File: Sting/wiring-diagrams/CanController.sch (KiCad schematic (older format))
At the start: 57 parts

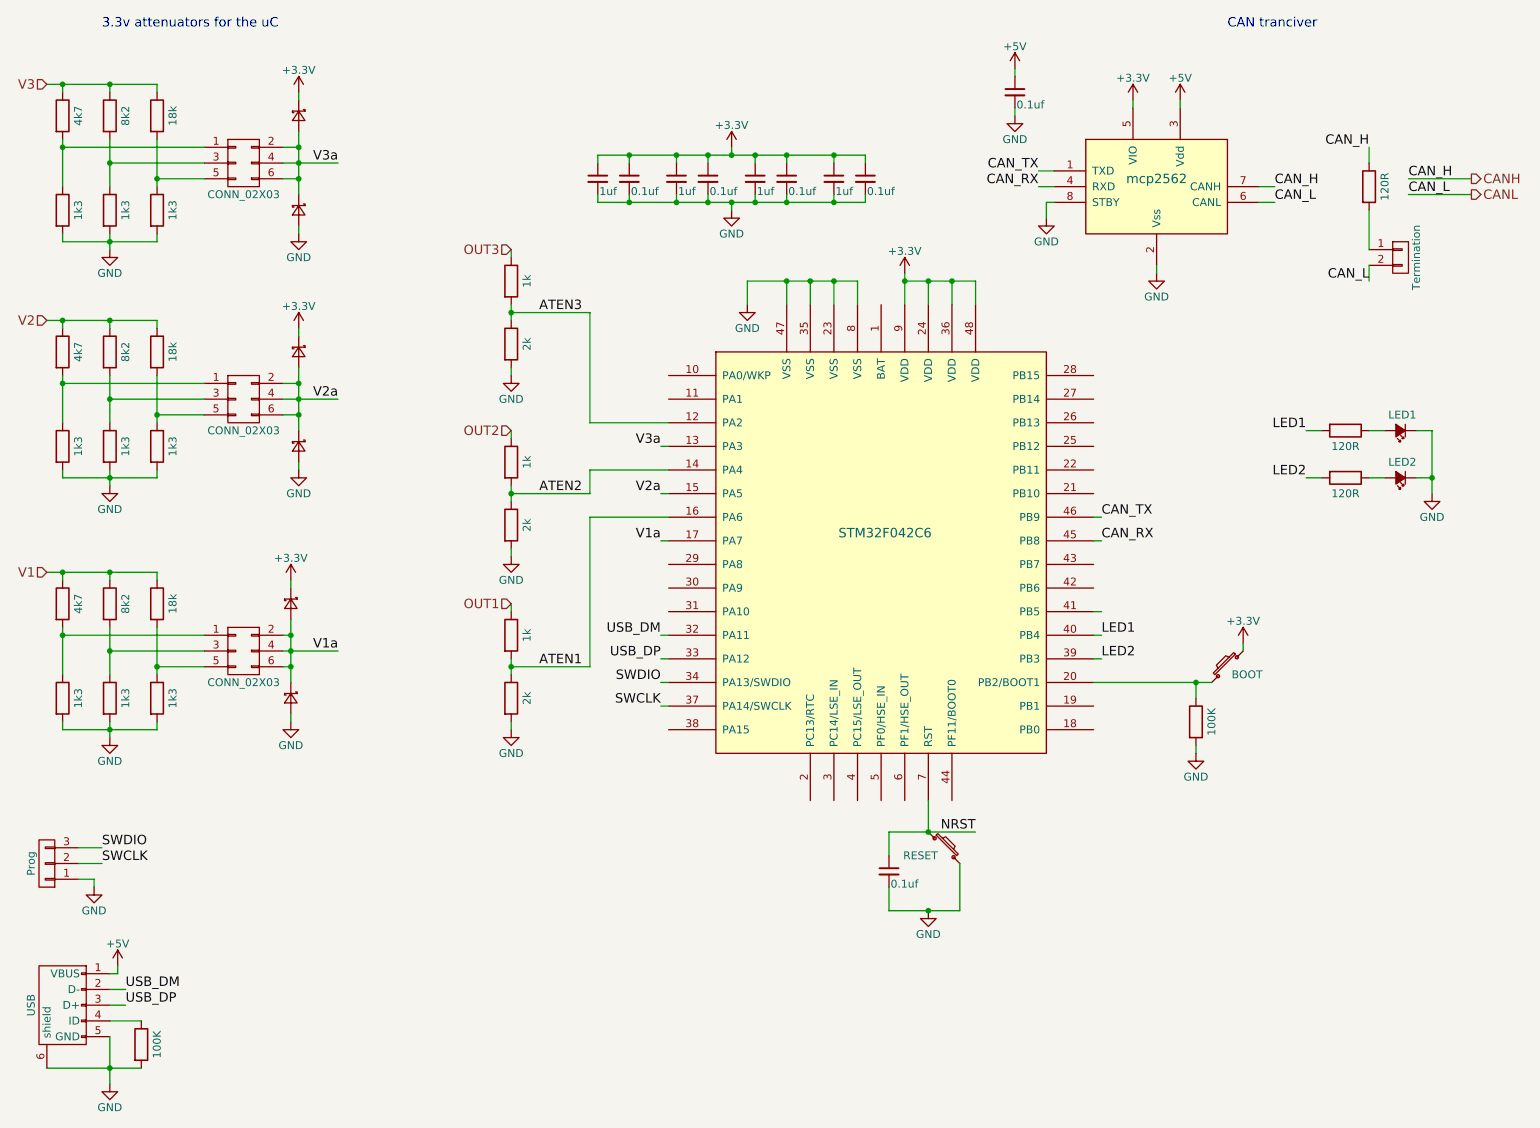
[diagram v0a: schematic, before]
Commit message: fixed missing parts updated sensor boards
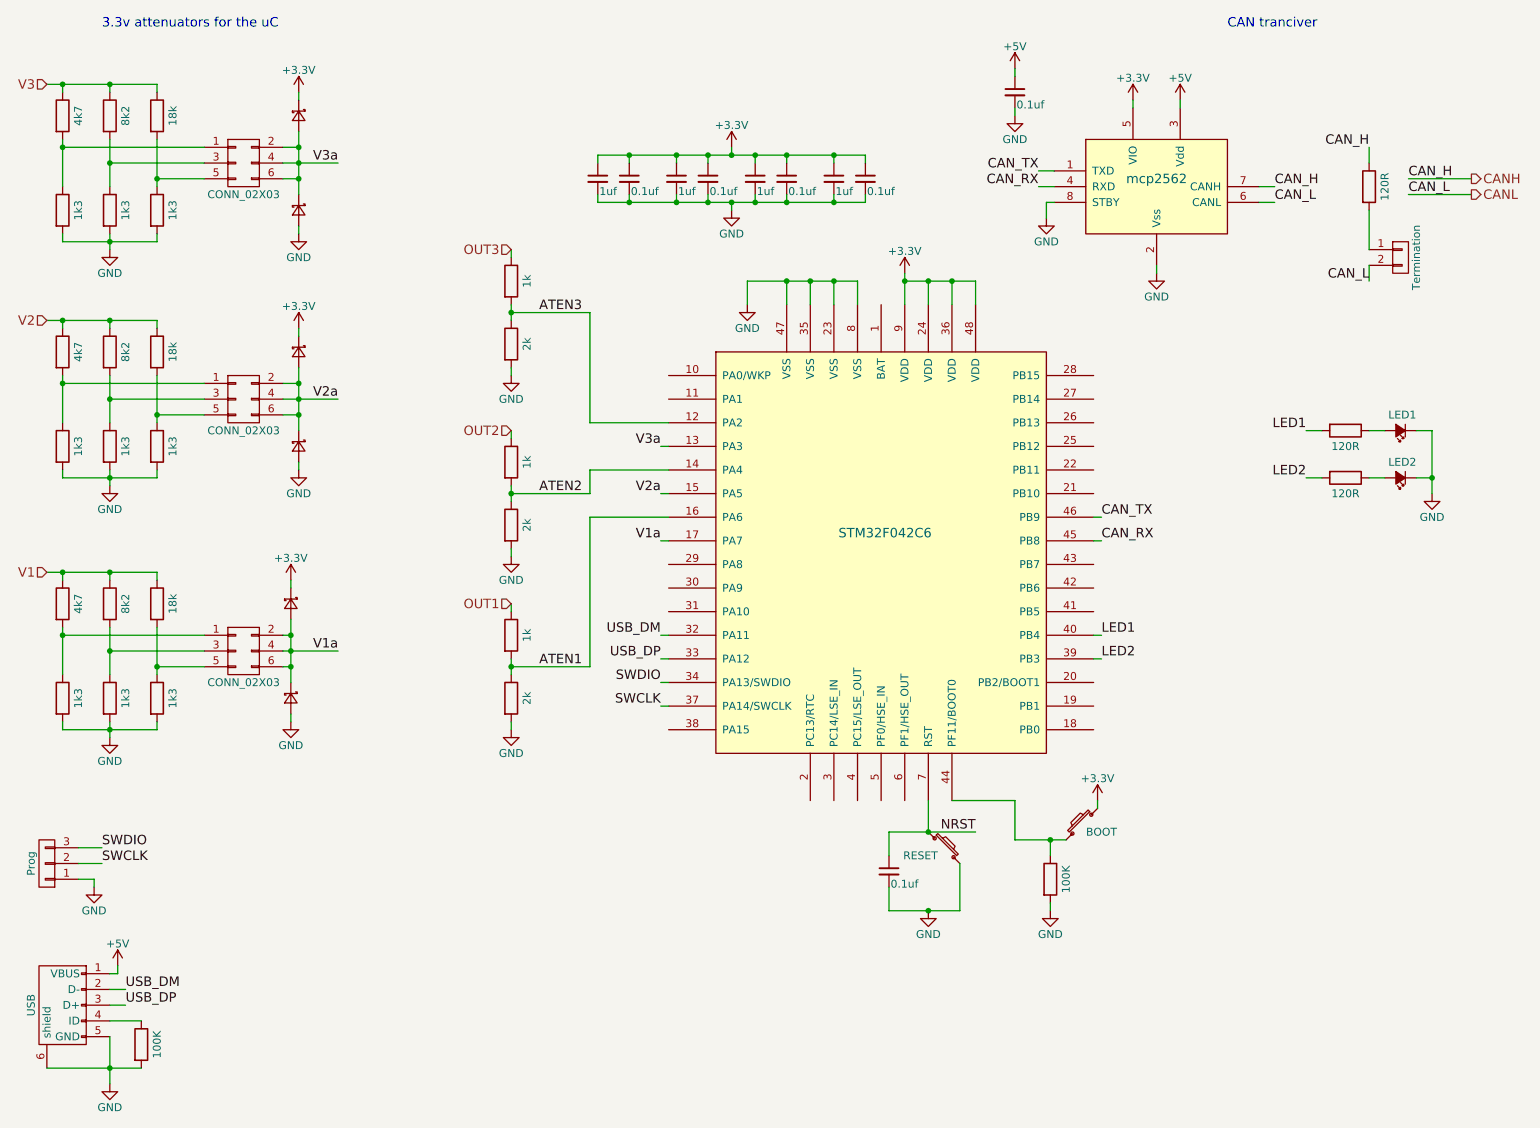
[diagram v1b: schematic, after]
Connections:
- net at R?.1, SW?.2: now also U?.44 (PF11/BOOT0); no longer U?.20 (PB2/BOOT1)

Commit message: Moved where the relay to turn on the starter relay gets power from
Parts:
- P?: symbol USB_OTG -> USB_OTG-RESCUE-Wiring_Diagram_v2
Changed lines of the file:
@@
 EESchema Schematic File Version 2
+LIBS:Wiring Diagram v2-rescue
 LIBS:power
 LIBS:device
@@
 $EndComp
 $Comp
-L USB_OTG P?
+L USB_OTG-RESCUE-Wiring_Diagram_v2 P?
 U 1 1 58900FF7
 P 1100 7000
